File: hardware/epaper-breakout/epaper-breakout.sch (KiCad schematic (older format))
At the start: 107 parts, among them J1 USB_C_16P, J2 Conn_02x06_Counter_Clockwise, Q1 AO3401A, Q2 MMBT3904, Q3 MMBT3904, Q4 MMBT3904, Q5 2N7002, Q6 AO3401A, Q7 AO3401A, SW1 SW_DIP_x01, U1 LT1945, U10 ESP32-WROVER, U11 PCF8563T, U12 MCP9700AT-ETT, U13 ED060XC5, U14 FPC-TOUCH, U2 LT1945, U3 XC6206PxxxMR, U4 CH340C, U5 74HC4094-normal, U6 LM358, U7 CONN-Battery, U8 TP4056, U9 MCP1700-3302E_SOT23, Y1 Crystal

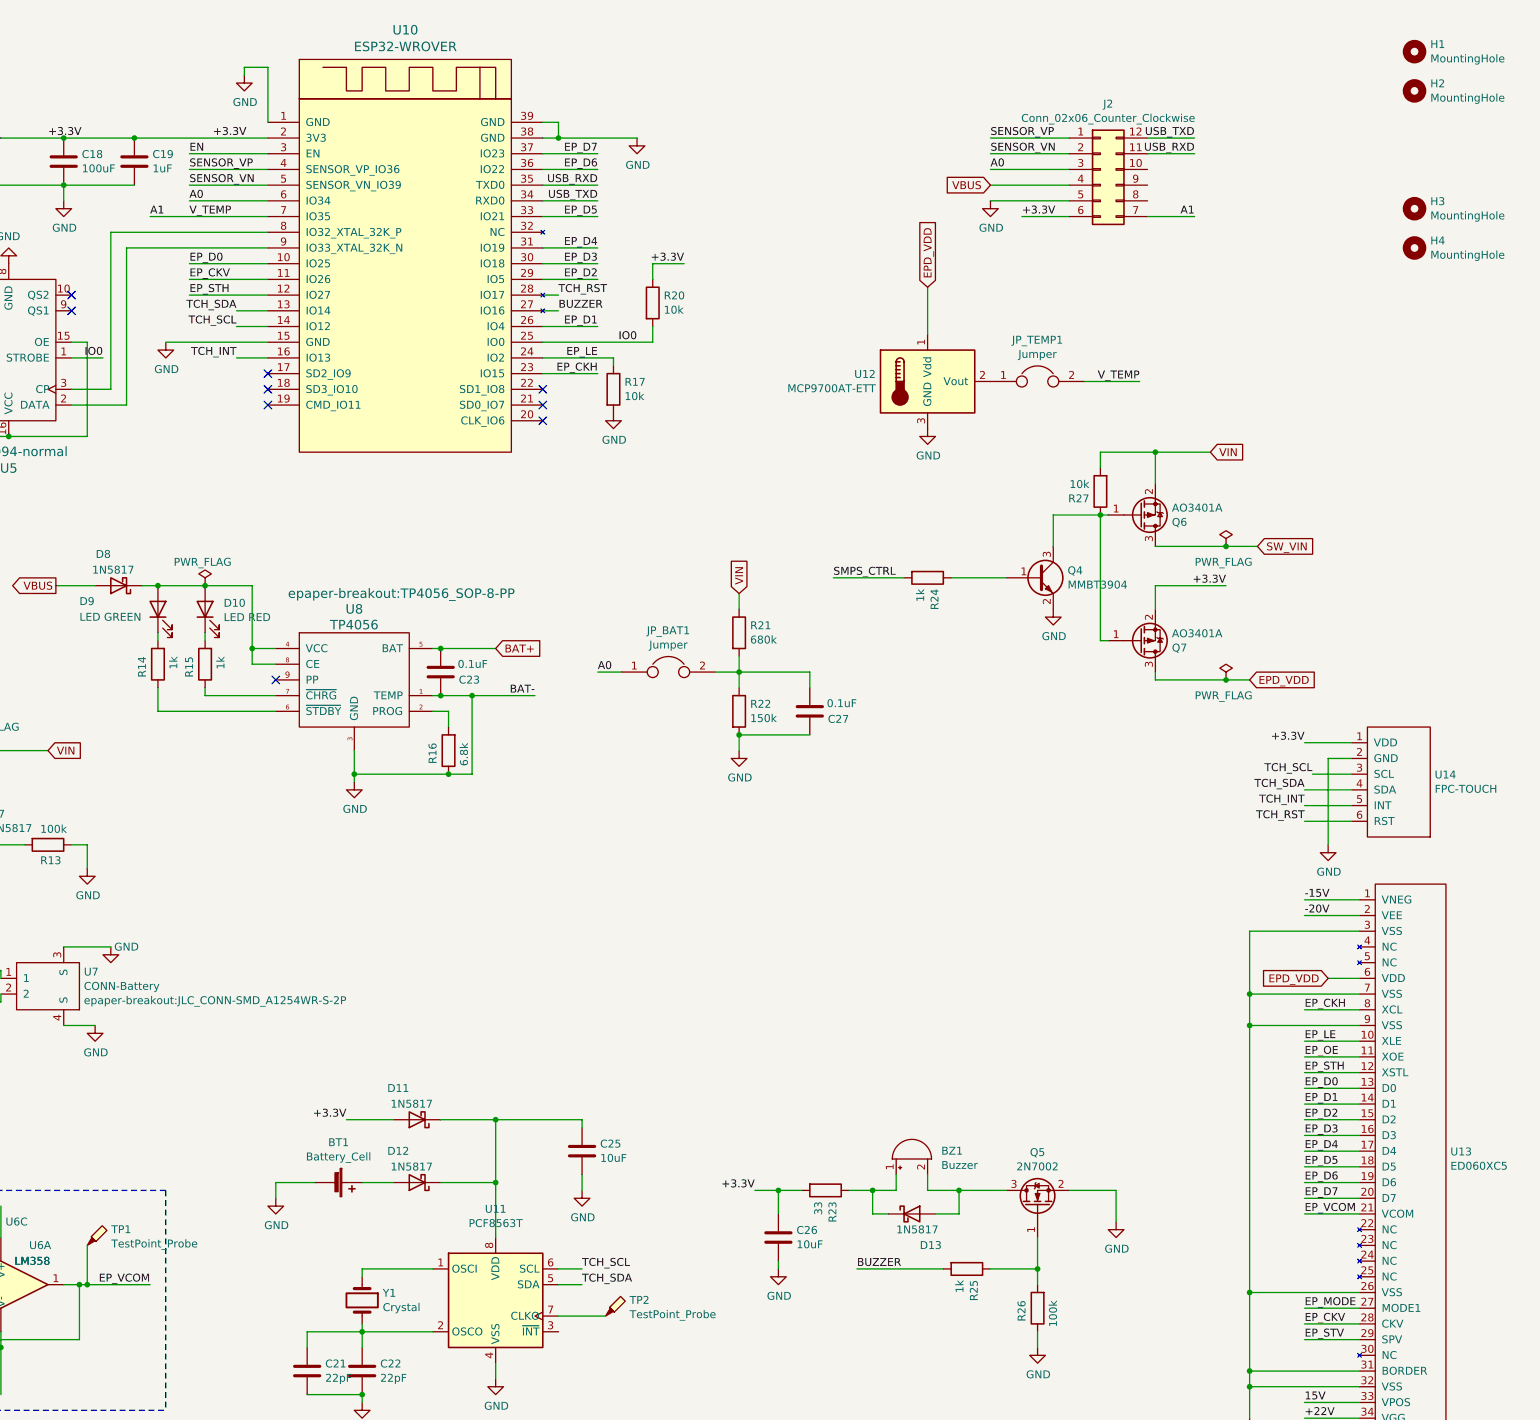
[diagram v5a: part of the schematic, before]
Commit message: change usb-c type
2022-08-27
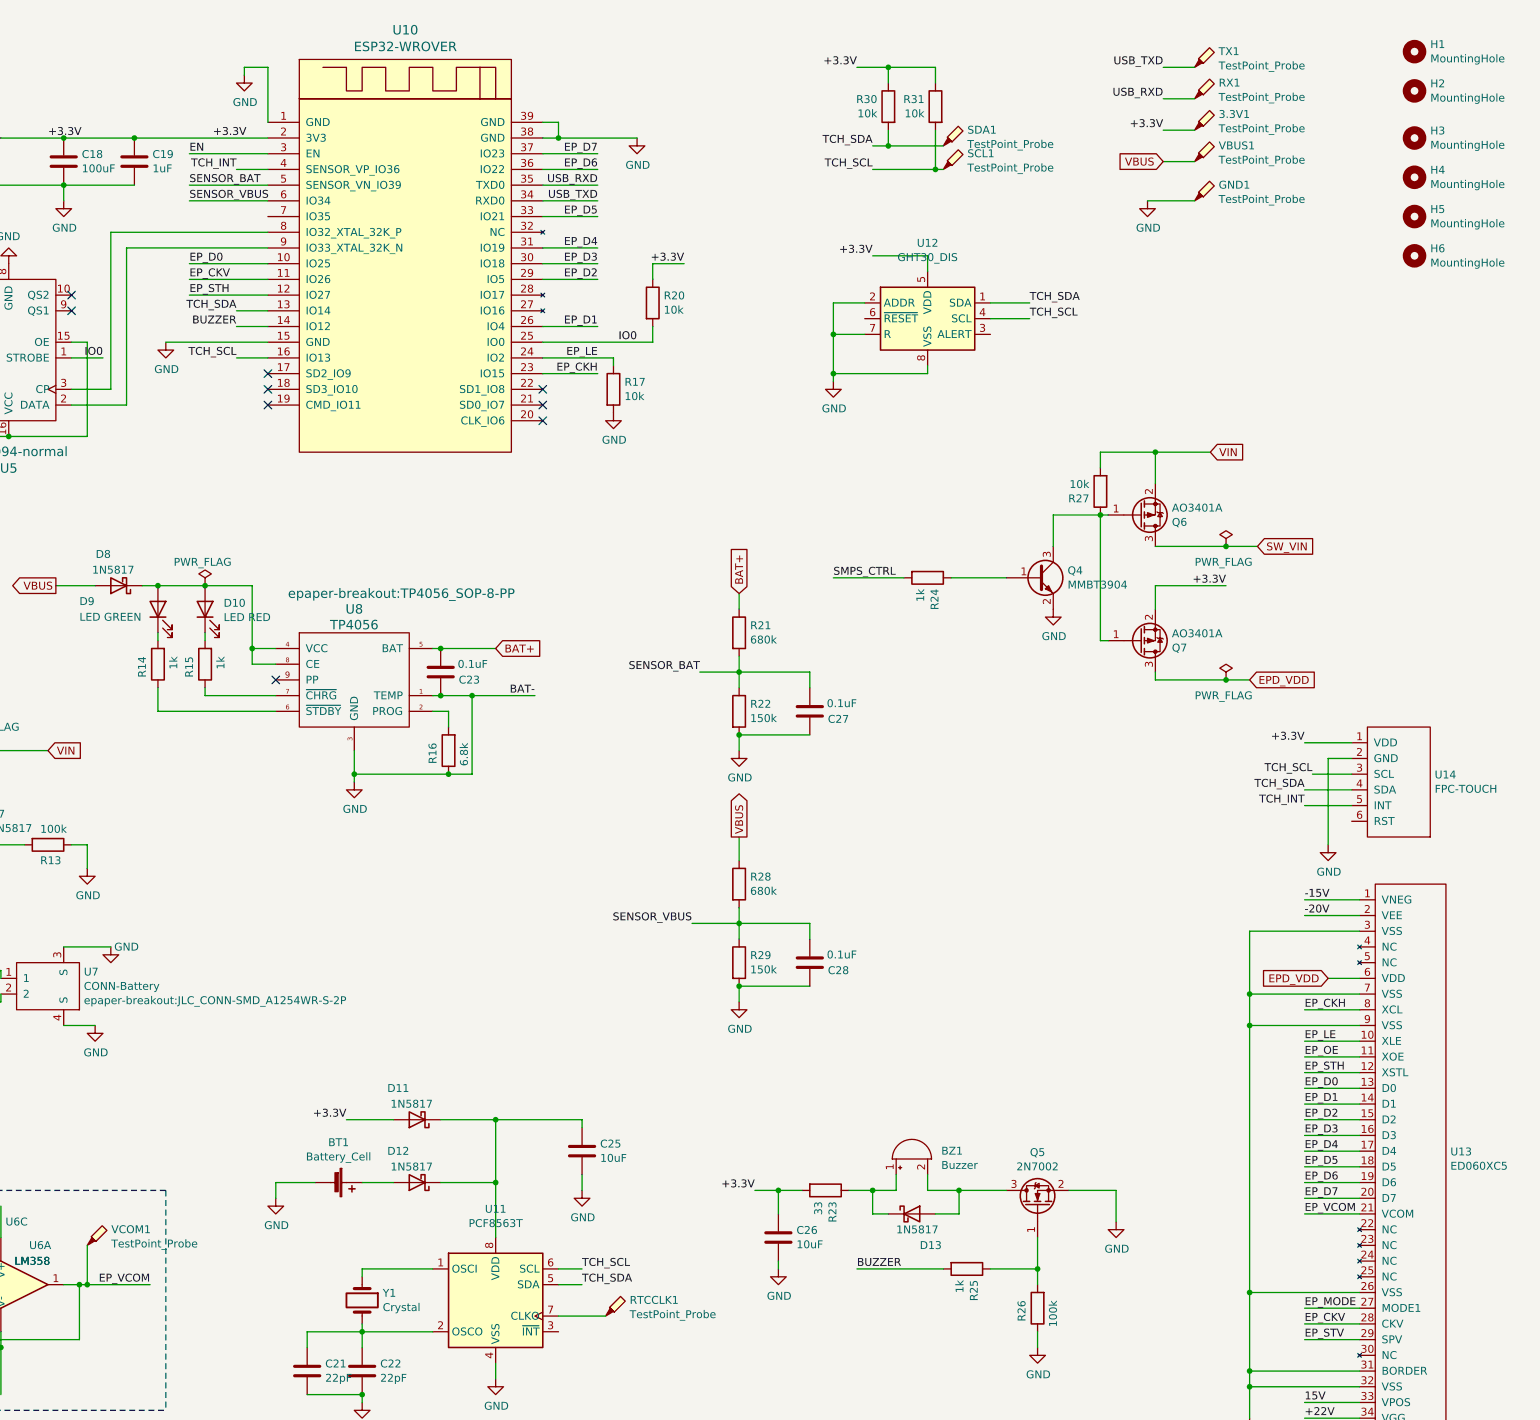
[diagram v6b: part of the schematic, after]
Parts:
- removed J2: Conn_02x06_Counter_Clockwise, Connector_PinHeader_2.54mm:PinHeader_2x06_P2.54mm_Vertical, symbol Connector_Generic:Conn_02x06_Counter_Clockwise
- removed JP_BAT1, JP_TEMP1: Jumper, Jumper:SolderJumper-2_P1.3mm_Bridged2Bar_RoundedPad1.0x1.5mm, symbol Device:Jumper
- removed U12: MCP9700AT-ETT, Package_TO_SOT_SMD:SOT-23, symbol Sensor_Temperature:MCP9700AT-ETT
- added 3.3V1, GND1, RX1, SCL1, SDA1, TX1, VBUS1: TestPoint_Probe, TestPoint:TestPoint_Pad_D1.0mm, symbol Connector:TestPoint_Probe
- added C28: 0.1uF, Capacitor_SMD:C_0603_1608Metric, symbol Device:C
- added H5, H6: MountingHole, MountingHole:MountingHole_2.2mm_M2, symbol Mechanical:MountingHole
- added R28: 680k, Resistor_SMD:R_0805_2012Metric, symbol Device:R
- added R29: 150k, Resistor_SMD:R_0805_2012Metric, symbol Device:R
- added R30, R31: 10k, Resistor_SMD:R_0805_2012Metric, symbol Device:R
- added U12: GHT30_DIS, Sensor_Humidity:Sensirion_DFN-8-1EP_2.5x2.5mm_P0.5mm_EP1.1x1.7mm, symbol epd_breakout:GHT30-DIS
- H3, H4: footprint MountingHole:MountingHole_4mm -> MountingHole:MountingHole_2.2mm_M2
- J1: footprint epaper-breakout:JLC_USB-C-SMD_KH-TYPE-C-16P -> epaper-breakout:JLC_USB-C-SMD_TYPE-C-31-M-13C; LCSC C709357 -> C2835312
- renumbered TP2 to RTCCLK1, TP1 to VCOM1
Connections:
- net SENSOR_VN is gone; now on net SENSOR_BAT: U10.5 (SENSOR_VN_IO39)
- net SENSOR_VP is gone; now on net TCH_INT: U10.4 (SENSOR_VP_IO36)
- net +3.3V: now also 3.3V1.1, R30.1, R31.1, U12.5 (VDD)
- net BAT+: now also R21.1
- net BUZZER: now also U10.14 (IO12); no longer U10.27 (IO16)
- net GND: now also C28.1, GND1.1, R29.2, U12.2 (ADDR), U12.7 (R), U12.8 (VSS), U12.9 (VSS)
- net TCH_INT: no longer U10.16 (IO13)
- net TCH_SCL: now also U10.16 (IO13), R31.2, SCL1.1, U12.4 (SCL); no longer U10.14 (IO12)
- net TCH_SDA: now also R30.2, SDA1.1, U12.1 (SDA)
- net USB_RXD: now also RX1.1
- net USB_TXD: now also TX1.1
- net VBUS: now also R28.1, VBUS1.1
- net VIN: no longer R21.1
- net SENSOR_BAT: now reaches C27.2, R21.2, R22.1
- net A0 renamed SENSOR_VBUS
- net SENSOR_VBUS: now also C28.2, R28.2, R29.1
- net A1: no longer names the net of U10.7 (IO35)
- net TCH_RST: no longer names the net of U10.28 (IO17)
- net TCH_RST: no longer U14.6 (RST)
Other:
- moved on the sheet: H3, H4

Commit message: change FPC connector
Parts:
- U13: footprint epaper-breakout:X05A20H34G -> epaper-breakout:JLC_FFC-SMD_34P-P0.50_FH34SRJ-34S-0.5SH
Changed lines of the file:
@@
 F 0 "U13" H 15528 7946 50  0000 L CNN
 F 1 "ED060XC5" H 15528 7855 50  0000 L CNN
-F 2 "epaper-breakout:X05A20H34G" H 15000 9750 50  0001 C CNN
+F 2 "epaper-breakout:JLC_FFC-SMD_34P-P0.50_FH34SRJ-34S-0.5SH" H 15000 9750 50  0001 C CNN
 F 3 "http://www.universaldisplay.asia/wp-content/uploads/2012/10/ED060XC5.pdf, https://datasheet.lcsc.com/szlcsc/2005221833_XKB-Connectivity-X05A20H34G_C528053.pdf" H 15000 9750 50  0001 C CNN
 F 4 "C528053" H 14950 7900 50  0001 C CNN "LCSC"
